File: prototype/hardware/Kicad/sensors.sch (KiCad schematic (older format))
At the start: 14 parts, among them U1 LSM9DS1, U5 H3LIS100DL, U8 MS5607-02BA

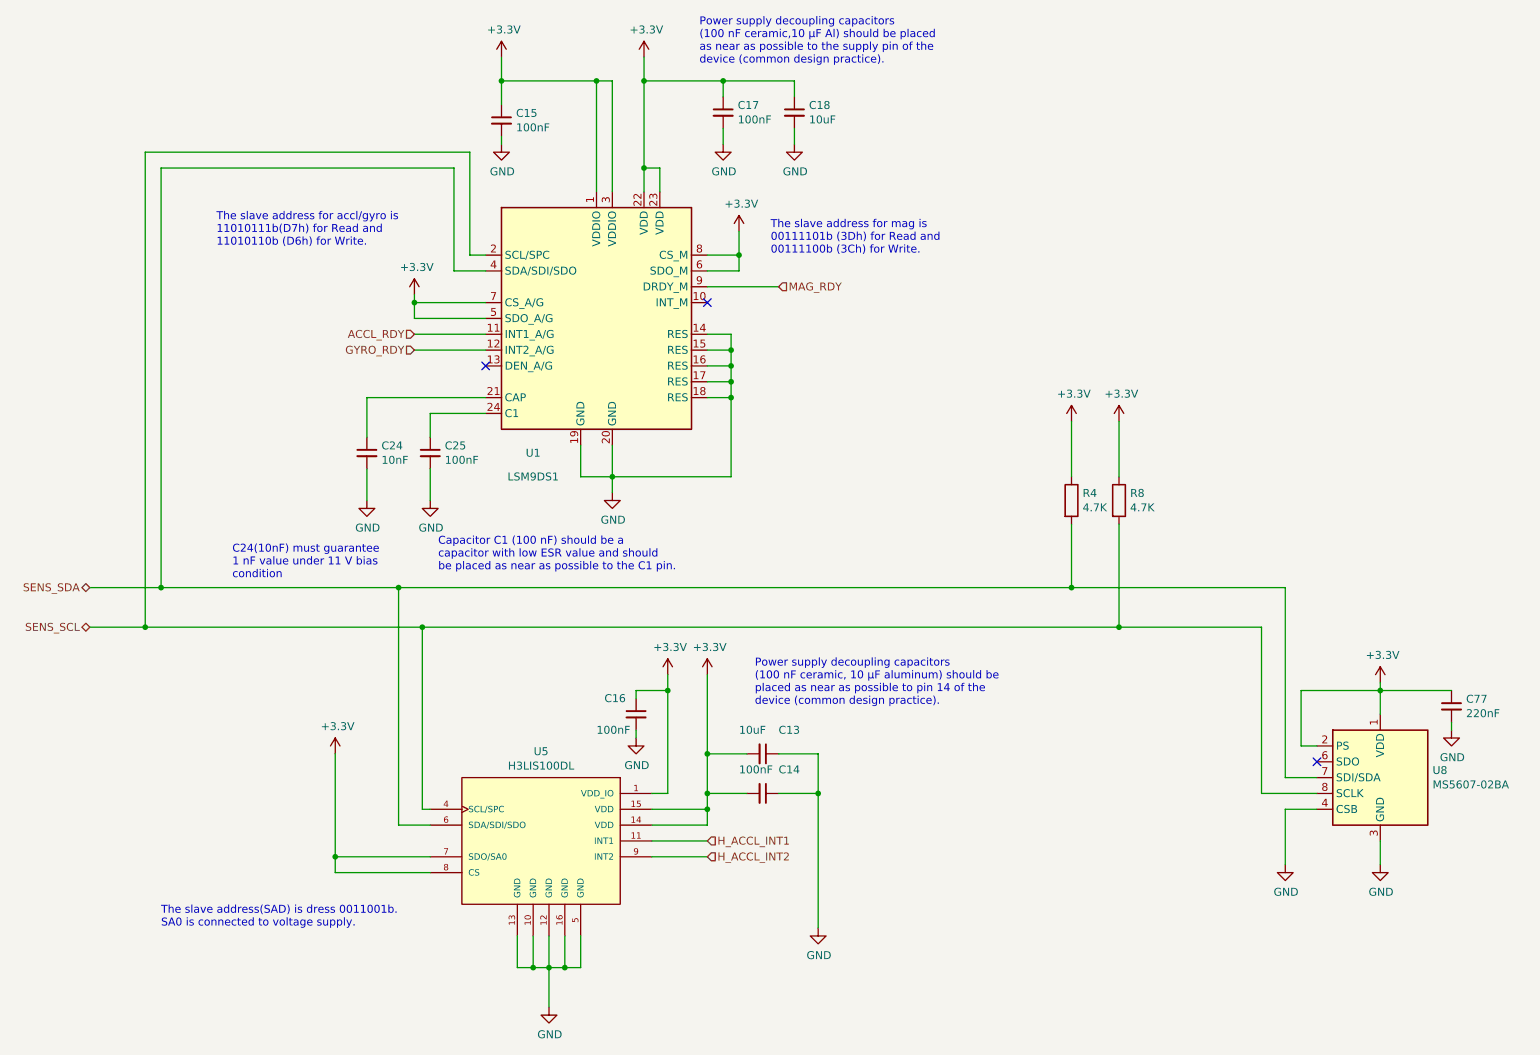
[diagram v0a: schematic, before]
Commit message: removed the samd21 and put in the murata
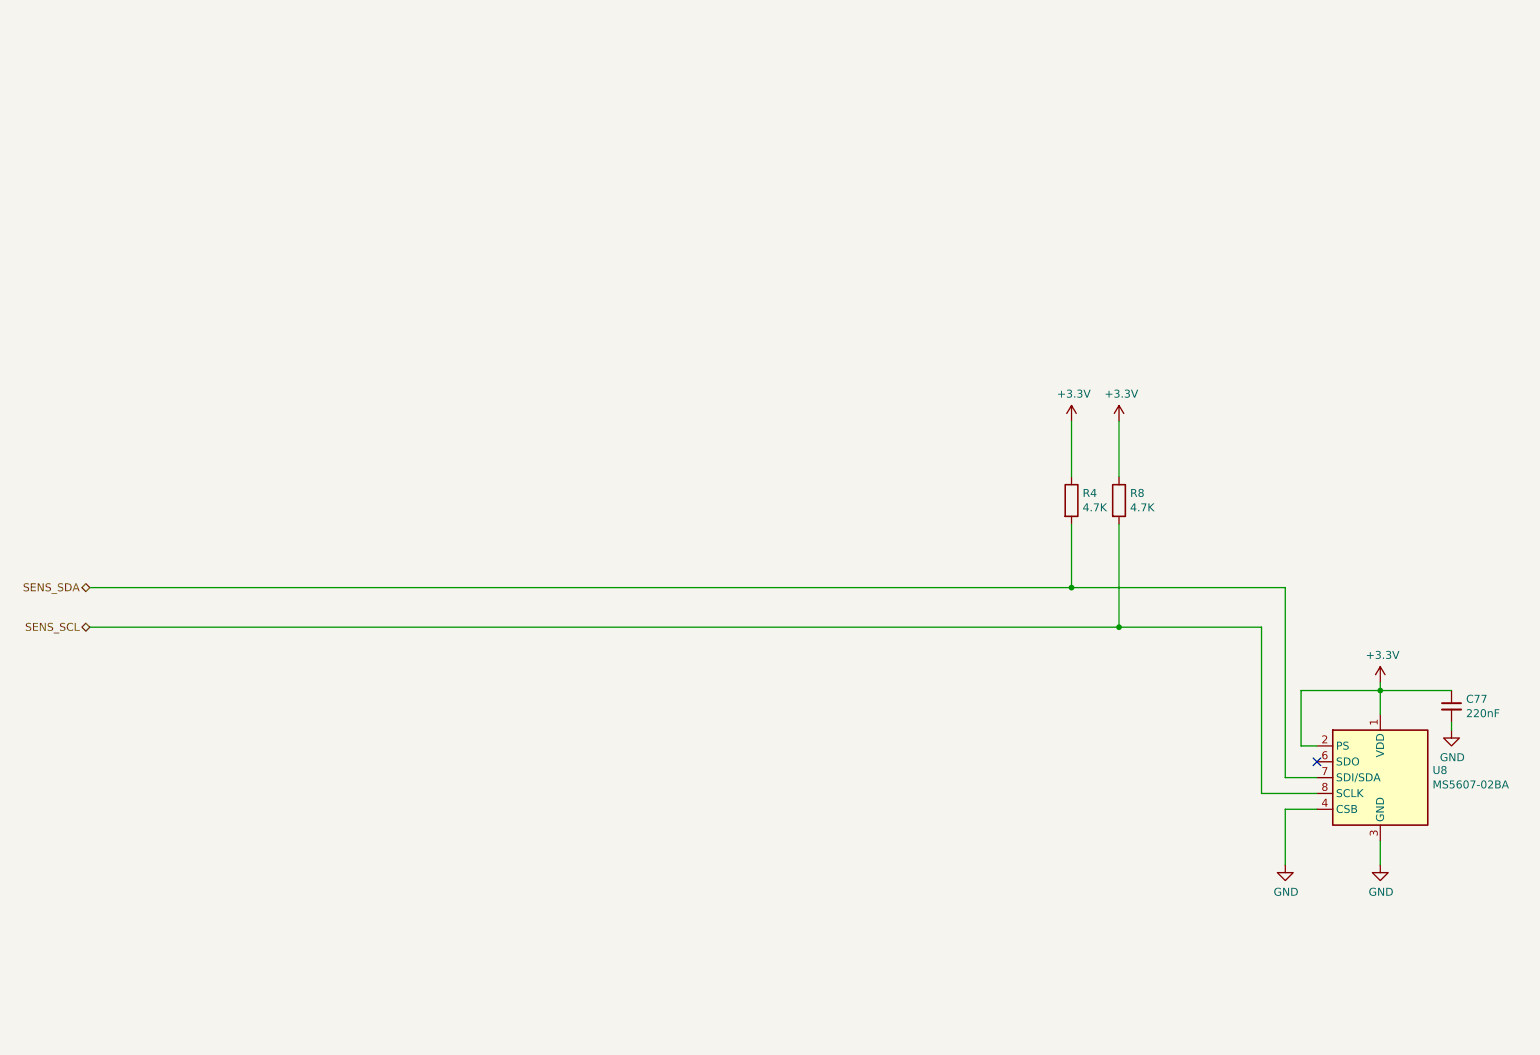
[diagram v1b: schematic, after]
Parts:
- removed C13, C18: 10uF, Capacitor_SMD:C_0603_1608Metric, symbol Device:C_Small
- removed C14, C15, C16, C17, C25: 100nF, Capacitor_SMD:C_0603_1608Metric, symbol Device:C_Small
- removed C24: 10nF, Capacitor_SMD:C_0603_1608Metric, symbol Device:C_Small
- removed U1: LSM9DS1, Package_LGA:LGA-24L_3x3.5mm_P0.43mm, symbol Sensor_Motion:LSM9DS1
- removed U5: H3LIS100DL, flight-computer:TFLGA-16_3x3mm, symbol flight-computer:H3LIS100DL
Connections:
- no-connect marks 3 -> 1
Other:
- note removed: "C24(10nF) must guarantee \n1 nF value under 11 V bias \ncondition"
- note removed: "Capacitor C1 (100 nF) should be a \ncapacitor with low ESR value and should \nbe placed as near as possible to the C1 pin."
- note removed: "Power supply decoupling capacitors \n(100 nF ceramic, 10 μF aluminum) should be \nplaced as near as possible to pin 14 of the \ndevice (common design practice)."
- note removed: "Power supply decoupling capacitors \n(100 nF ceramic,10 μF Al) should be placed \nas near as possible to the supply pin of the \ndevice (common design practice)."
- note removed: "The slave address for accl/gyro is \n11010111b(D7h) for Read and \n11010110b (D6h) for Write."
- note removed: "The slave address for mag is \n00111101b (3Dh) for Read and \n00111100b (3Ch) for Write."
- note removed: "The slave address(SAD) is dress 0011001b.\nSA0 is connected to voltage supply."
